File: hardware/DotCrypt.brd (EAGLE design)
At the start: 12 x 33.1 mm, 15 parts, among them CN1 1X4-BIG, U1 ATMEGA328P-MU-QFN32, U3 ATSHA204-TSU

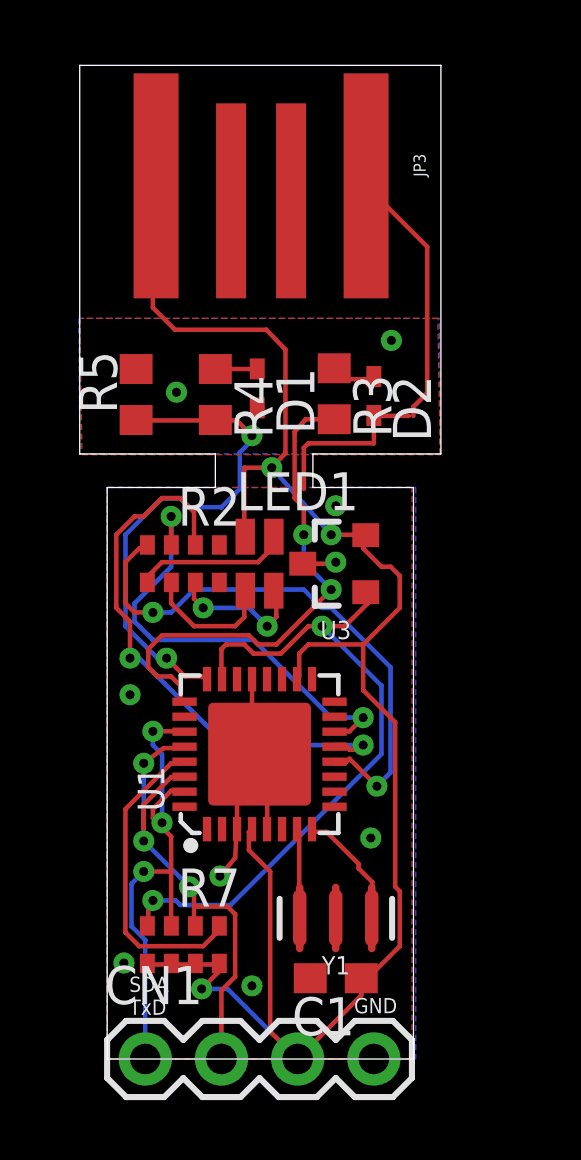
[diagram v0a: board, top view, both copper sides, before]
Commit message: Rearrange logos and pin connections
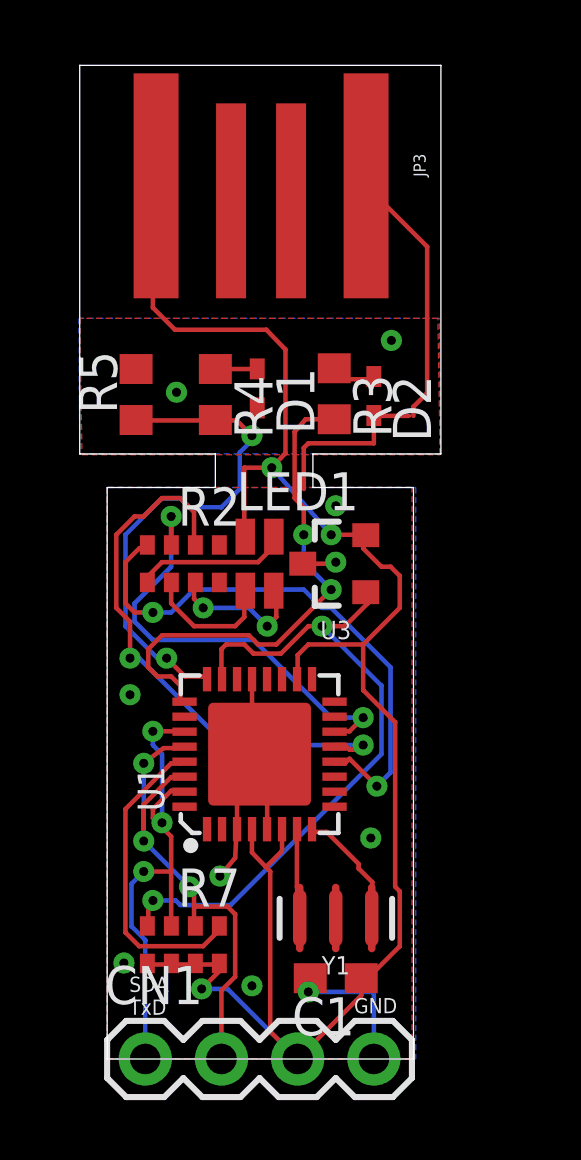
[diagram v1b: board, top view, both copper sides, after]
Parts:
- moved LOGO1 2.52 mm to (5.08, 5.77)
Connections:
- net +3V3: now also U1.6
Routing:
- net GND: track 26.4 -> 31.3 mm, vias 9 -> 10
- net +3V3: track 61.9 -> 63.3 mm
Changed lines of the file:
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@@
 <layer number="155" name="FabDoc3" color="7" fill="15" visible="no" active="no"/>
 <layer number="199" name="Contour" color="7" fill="1" visible="no" active="yes"/>
-<layer number="200" name="200bmp" color="1" fill="10" visible="yes" active="yes"/>
+<layer number="200" name="200bmp" color="1" fill="10" visible="no" active="yes"/>
 <layer number="201" name="201bmp" color="2" fill="1" visible="no" active="no"/>
 <layer number="202" name="202bmp" color="3" fill="1" visible="no" active="no"/>
@@
 TxD</text>
 <text x="8.2296" y="2.794" size="0.508" layer="21">GND</text>
-<text x="0" y="18.8722" size="0.508" layer="22" rot="MR180">DotCrypt v0.1.1</text>
-<text x="1.27" y="17.907" size="0.508" layer="22" rot="MR180">01/2018</text>
+<text x="9.4996" y="7.4168" size="0.508" layer="22" rot="SMR270">01/2018</text>
+<text x="7.4676" y="5.7658" size="0.508" layer="22" rot="SMR270" align="center">DotCrypt
+v0.1.1</text>
 </plain>
 <attributes>
@@
 <element name="R5" library="rcl" package="R0603" value="1.5kΩ" x="0.9652" y="23.4188" rot="R90"/>
 <element name="JP3" library="Spark" package="USB-A-PCB" value="USBPCB" x="5.1308" y="30.1752" rot="R270"/>
-<element name="LOGO1" library="SparkFun-Aesthetics" package="OSHW-LOGO-S" value="OSHW-LOGOS" x="7.5946" y="5.9436" rot="MR270"/>
+<element name="LOGO1" library="SparkFun-Aesthetics" package="OSHW-LOGO-S" value="OSHW-LOGOS" x="5.08" y="5.7658" rot="MR270"/>
 </elements>
 <signals>
@@
 <wire x1="8.89" y1="21.7932" x2="8.89" y2="22.7188" width="0.1524" layer="1"/>
 <wire x1="10.2108" y1="22.7076" x2="10.2108" y2="23.0124" width="0.1524" layer="1"/>
+<wire x1="6.77" y1="3.9624" x2="6.7056" y2="3.9624" width="0.1524" layer="1"/>
+<wire x1="6.7056" y1="3.9624" x2="6.7056" y2="3.5052" width="0.1524" layer="1"/>
+<via x="6.7056" y="3.5052" extent="1-16" drill="0.3"/>
+<wire x1="6.7056" y1="3.5052" x2="8.89" y2="3.5052" width="0.1524" layer="16"/>
+<wire x1="8.89" y1="3.5052" x2="8.89" y2="1.27" width="0.1524" layer="16"/>
 </signal>
 <signal name="SCK">
@@
 <contactref element="C1" pad="1"/>
 <contactref element="JP3" pad="5V"/>
-<wire x1="6.4008" y1="14.7828" x2="6.4008" y2="14.0208" width="0.1524" layer="1"/>
-<wire x1="6.7056" y1="15.0876" x2="6.4008" y2="14.7828" width="0.1524" layer="1"/>
+<wire x1="6.35" y1="14.732" x2="6.35" y2="14.0208" width="0.1524" layer="1"/>
+<wire x1="6.7056" y1="15.0876" x2="6.35" y2="14.732" width="0.1524" layer="1"/>
 <wire x1="8.5344" y1="15.0876" x2="6.7056" y2="15.0876" width="0.1524" layer="1"/>
 <wire x1="9.7536" y1="16.3068" x2="8.5344" y2="15.0876" width="0.1524" layer="1"/>
@@
 <wire x1="8.5344" y1="18.288" x2="9.144" y2="17.6784" width="0.1524" layer="1"/>
 <wire x1="8.5344" y1="18.5928" x2="8.5344" y2="18.288" width="0.1524" layer="1"/>
-<wire x1="6.4008" y1="14.0208" x2="6.33" y2="13.93" width="0.1524" layer="1"/>
+<wire x1="6.35" y1="14.0208" x2="6.33" y2="13.93" width="0.1524" layer="1"/>
 <wire x1="8.5344" y1="18.5928" x2="8.62" y2="18.73" width="0.1524" layer="1"/>
 <wire x1="2.1336" y1="4.4196" x2="1.3716" y2="4.4196" width="0.1524" layer="1"/>
@@
 <wire x1="3.6576" y1="4.4196" x2="3.74" y2="4.455" width="0.1524" layer="1"/>
 <wire x1="3.048" y1="4.4196" x2="2.94" y2="4.455" width="0.1524" layer="1"/>
-<wire x1="4.7244" y1="8.8392" x2="4.83" y2="8.93" width="0.1524" layer="1"/>
+<wire x1="4.826" y1="8.763" x2="4.83" y2="8.93" width="0.1524" layer="1"/>
 <wire x1="3.81" y1="4.4196" x2="3.74" y2="4.455" width="0.1524" layer="1"/>
 <wire x1="6.2484" y1="1.6764" x2="7.0104" y2="1.6764" width="0.1524" layer="1"/>
@@
 <wire x1="6.2484" y1="1.6764" x2="6.2484" y2="1.3716" width="0.1524" layer="1"/>
 <wire x1="6.2484" y1="1.3716" x2="6.35" y2="1.27" width="0.1524" layer="1"/>
-<wire x1="4.7244" y1="8.8392" x2="4.7244" y2="8.2296" width="0.1524" layer="1"/>
-<wire x1="4.7244" y1="8.2296" x2="5.4356" y2="7.5184" width="0.1524" layer="1"/>
+<wire x1="4.826" y1="8.763" x2="4.826" y2="8.1534" width="0.1524" layer="1"/>
+<wire x1="4.826" y1="8.1534" x2="5.291446875" y2="7.668559375" width="0.1524" layer="1"/>
+<wire x1="5.291446875" y1="7.668559375" x2="5.4356" y2="7.5184" width="0.1524" layer="1"/>
 <wire x1="5.4356" y1="7.5184" x2="5.4356" y2="2.1844" width="0.1524" layer="1"/>
 <wire x1="5.4356" y1="2.1844" x2="6.35" y2="1.27" width="0.1524" layer="1"/>
@@
 <wire x1="5.9436" y1="21.463" x2="5.4864" y2="20.9804" width="0.1524" layer="1"/>
 <wire x1="5.9436" y1="24.9174" x2="5.9436" y2="21.463" width="0.1524" layer="1"/>
+<contactref element="U1" pad="6"/>
+<wire x1="5.83" y1="8.93" x2="5.83" y2="8.2071125" width="0.1524" layer="1"/>
+<wire x1="5.83" y1="8.2071125" x2="5.291446875" y2="7.668559375" width="0.1524" layer="1"/>
 </signal>
 <signal name="PUSH">
@@
 <contactref element="U1" pad="7"/>
 <contactref element="Y1" pad="3"/>
-<wire x1="6.4008" y1="7.0104" x2="6.4008" y2="8.8392" width="0.1524" layer="1"/>
-<wire x1="6.4008" y1="8.8392" x2="6.33" y2="8.93" width="0.1524" layer="1"/>
-<wire x1="6.4008" y1="7.0104" x2="6.42" y2="5.969" width="0.1524" layer="1"/>
+<wire x1="6.3246" y1="7.0104" x2="6.3246" y2="8.8392" width="0.1524" layer="1"/>
+<wire x1="6.3246" y1="8.8392" x2="6.33" y2="8.93" width="0.1524" layer="1"/>
+<wire x1="6.3246" y1="7.0104" x2="6.42" y2="5.969" width="0.1524" layer="1"/>
 </signal>
 <signal name="XTAL2">

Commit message: Add USB D+ D- connections
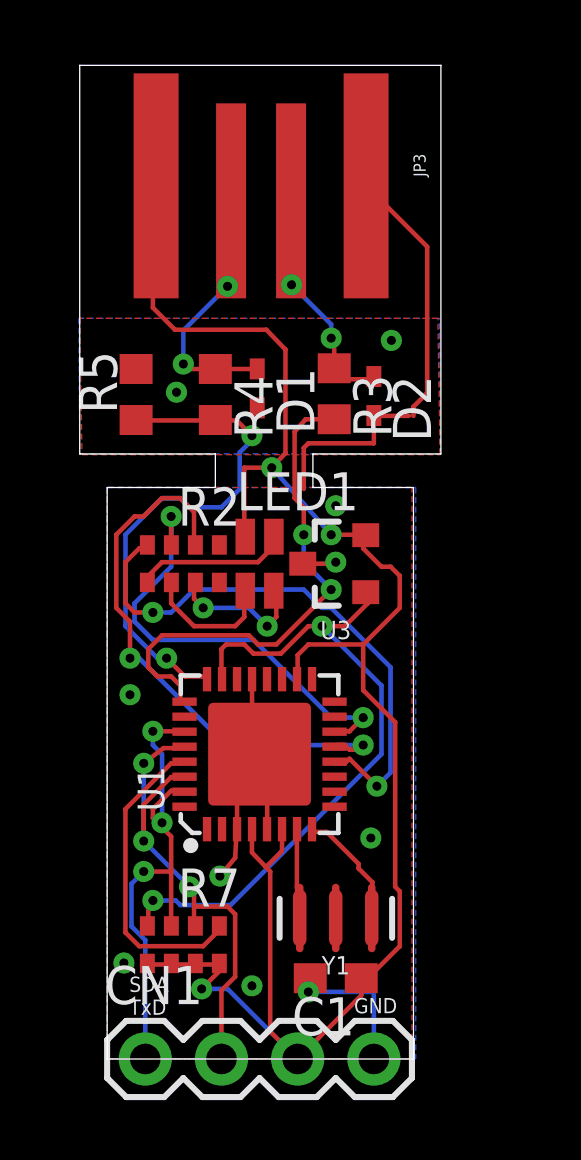
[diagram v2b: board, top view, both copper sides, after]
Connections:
- net USB_D+: now also JP3.USB_P
- net USB_D-: now also JP3.USB_M
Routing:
- net USB_D-: track 1.40 -> 8.63 mm, vias 0 -> 2
- net USB_D+: track 1.54 -> 7.72 mm, vias 0 -> 2
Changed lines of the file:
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@@
 <wire x1="3.6068" y1="24.2688" x2="4.9998" y2="24.2688" width="0.1524" layer="1"/>
 <wire x1="4.9998" y1="24.2688" x2="5.0038" y2="24.2728" width="0.1524" layer="1"/>
+<contactref element="JP3" pad="USB_M"/>
+<wire x1="3.6068" y1="24.2688" x2="2.706" y2="24.2688" width="0.1524" layer="1"/>
+<wire x1="2.706" y1="24.2688" x2="2.54" y2="24.4348" width="0.1524" layer="1"/>
+<via x="2.54" y="24.4348" extent="1-16" drill="0.3"/>
+<wire x1="2.54" y1="24.4348" x2="2.54" y2="25.5524" width="0.1524" layer="16"/>
+<wire x1="2.54" y1="25.5524" x2="4.0132" y2="27.0256" width="0.1524" layer="16"/>
+<via x="4.0132" y="27.0256" extent="1-16" drill="0.3"/>
+<wire x1="4.0132" y1="27.0256" x2="4.0132" y2="29.7576" width="0.1524" layer="1"/>
+<wire x1="4.0132" y1="29.7576" x2="4.1308" y2="29.8752" width="0.1524" layer="1"/>
 </signal>
 <signal name="USB_D+">
@@
 <wire x1="8.8392" y1="23.9268" x2="7.8858" y2="23.9268" width="0.1524" layer="1"/>
 <wire x1="7.8858" y1="23.9268" x2="7.5692" y2="24.2942" width="0.1524" layer="1"/>
+<contactref element="JP3" pad="USB_P"/>
+<wire x1="7.5692" y1="24.2942" x2="7.5692" y2="25.1968" width="0.1524" layer="1"/>
+<wire x1="7.5692" y1="25.1968" x2="7.4676" y2="25.2984" width="0.1524" layer="1"/>
+<via x="7.4676" y="25.2984" extent="1-16" drill="0.3"/>
+<wire x1="7.4676" y1="25.2984" x2="7.4676" y2="25.7556" width="0.1524" layer="16"/>
+<wire x1="7.4676" y1="25.7556" x2="6.1468" y2="27.0764" width="0.1524" layer="16"/>
+<via x="6.1468" y="27.0764" extent="1-16" drill="0.3"/>
+<wire x1="6.1468" y1="27.0764" x2="6.1468" y2="29.8592" width="0.1524" layer="1"/>
+<wire x1="6.1468" y1="29.8592" x2="6.1308" y2="29.8752" width="0.1524" layer="1"/>
 </signal>
 </signals>

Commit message: Add 3V3 regulator
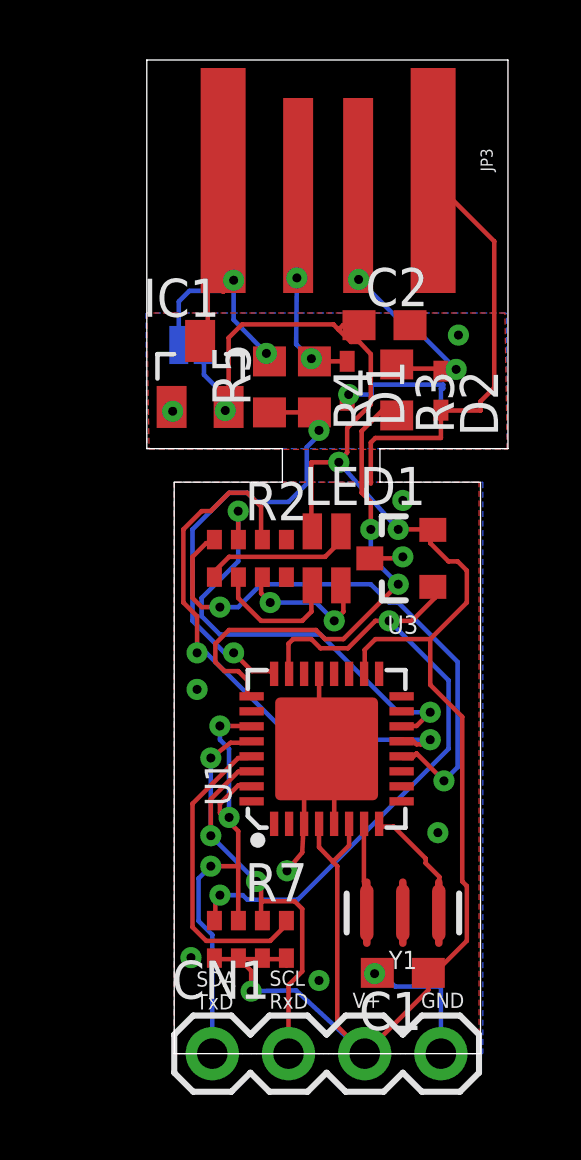
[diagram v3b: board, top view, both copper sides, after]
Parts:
- added C2: 1uF, rcl:C0603
- added IC1: MCP1703CB, linear:SOT23
- added JP1: JUMPER-SMT_2_NO_SILK, SparkFun-Jumpers:SMT-JUMPER_2_NO_SILK
- moved R5 4.45 mm to (5.41, 23.7)
- moved R4 3.31 mm to (6.91, 23.7)
- moved D1 3.01 mm to (8.00, 23.9)
- moved C1 2.24 mm to (9.86, 4.14)
- moved CN1 2.24 mm to (3.51, 1.45)
- moved JP3 2.24 mm to (7.37, 30.4)
- moved LED1 2.24 mm to (7.32, 18.0)
- moved LOGO1 2.24 mm to (7.32, 5.94)
- moved R2 2.24 mm to (4.78, 18.0)
- moved R7 2.24 mm to (4.78, 5.26)
- moved U1 2.24 mm to (7.32, 11.6)
- moved U3 2.24 mm to (9.86, 18.0)
- moved Y1 2.24 mm to (9.86, 6.15)
- moved D2 2.24 mm to (11.1, 23.6)
- moved R3 2.09 mm to (9.65, 23.6)
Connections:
- net +3V3: now also C2.1, IC1.2, JP1.1; no longer JP3.5V
- net +5V: now also IC1.3, JP1.2, JP3.5V
- net GND: now also C2.2, IC1.1
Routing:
- net +5V: track 0.00 -> 15.6 mm, vias 0 -> 2
- net GND: track 31.3 -> 36.0 mm, vias 10 -> 11
- net +3V3: track 63.3 -> 66.1 mm, vias 3 -> 4
- net USB_D+: track 7.72 -> 9.45 mm
- net USB_D-: track 8.63 -> 7.10 mm
- net D-: track 17.2 -> 16.0 mm
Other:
- board text added: "5V Logic"
- board text added: "SCL RxD"
- board text added: "V+"

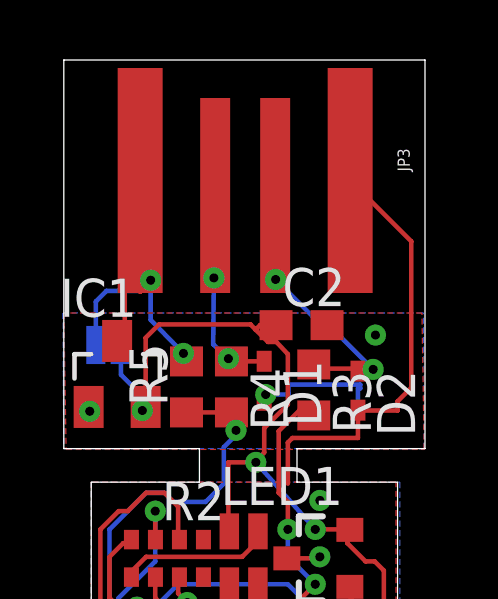
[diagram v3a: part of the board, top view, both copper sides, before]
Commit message: Reorder traces
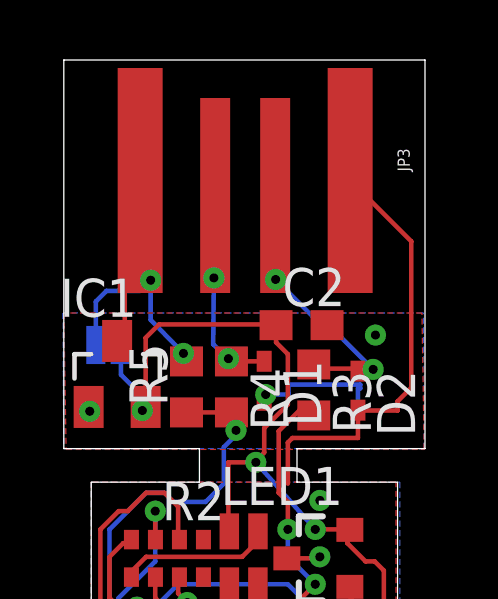
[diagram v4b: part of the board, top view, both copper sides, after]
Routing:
- net +5V: track 15.6 -> 12.5 mm
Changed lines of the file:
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@@
 <wire x1="10.7052" y1="4.1402" x2="10.7052" y2="3.5678" width="0.1524" layer="1"/>
 <wire x1="10.7052" y1="3.5678" x2="8.5852" y2="1.4478" width="0.1524" layer="1"/>
-<wire x1="4.4958" y1="25.7556" x2="7.5438" y2="25.7556" width="0.1524" layer="1"/>
-<wire x1="7.5438" y1="25.7556" x2="7.712678125" y2="25.579965625" width="0.1524" layer="1"/>
-<wire x1="7.712678125" y1="25.579965625" x2="8.128" y2="25.1714" width="0.1524" layer="1"/>
+<wire x1="4.4958" y1="25.7556" x2="8.3956" y2="25.7556" width="0.1524" layer="1"/>
 <wire x1="8.001" y1="21.4884" x2="7.7216" y2="21.1582" width="0.1524" layer="1"/>
 <contactref element="U1" pad="6"/>
@@
 <contactref element="C2" pad="1"/>
 <contactref element="IC1" pad="2"/>
-<wire x1="8.128" y1="25.1714" x2="8.4074" y2="25.1714" width="0.1524" layer="1"/>
-<wire x1="8.4074" y1="25.1714" x2="8.7884" y2="24.765" width="0.1524" layer="1"/>
 <wire x1="8.7884" y1="24.765" x2="8.7884" y2="23.0886" width="0.1524" layer="1"/>
 <wire x1="8.7884" y1="23.0886" x2="8.001" y2="22.3012" width="0.1524" layer="1"/>
@@
 <wire x1="4.4958" y1="25.7556" x2="4.0488" y2="25.3086" width="0.1524" layer="1"/>
 <wire x1="4.0488" y1="25.3086" x2="4.0488" y2="23.0046" width="0.1524" layer="1"/>
-<wire x1="8.3956" y1="25.7302" x2="7.865078125" y2="25.733078125" width="0.1524" layer="1"/>
-<wire x1="7.865078125" y1="25.733078125" x2="7.712678125" y2="25.579965625" width="0.1524" layer="1"/>
 <contactref element="JP1" pad="1"/>
 <wire x1="3.2004" y1="25.0698" x2="3.2258" y2="25.0698" width="0.1524" layer="16"/>
@@
 <wire x1="4.8006" y1="3.5306" x2="4.8006" y2="4.2074" width="0.1524" layer="1"/>
 <wire x1="4.8006" y1="4.2074" x2="4.3752" y2="4.6328" width="0.1524" layer="1"/>
+<wire x1="8.3956" y1="25.7556" x2="8.3956" y2="25.7302" width="0.1524" layer="1"/>
+<wire x1="8.7884" y1="24.765" x2="8.3956" y2="25.1578" width="0.1524" layer="1"/>
+<wire x1="8.3956" y1="25.1578" x2="8.3956" y2="25.7302" width="0.1524" layer="1"/>
 </signal>
 <signal name="PUSH">
@@
 <wire x1="4.2164" y1="25.908" x2="4.2164" y2="27.2288" width="0.1524" layer="16"/>
 <via x="4.2164" y="27.2288" extent="1-16" drill="0.3"/>
-<wire x1="4.2164" y1="27.2288" x2="3.866" y2="26.8426" width="0.1524" layer="1"/>
-<wire x1="3.866" y1="26.8426" x2="3.866" y2="29.4184" width="0.1524" layer="1"/>
 <contactref element="JP1" pad="2"/>
 <wire x1="2.3876" y1="25.0698" x2="2.3876" y2="26.5176" width="0.1524" layer="16"/>
@@
 <wire x1="2.7432" y1="26.8732" x2="3.8608" y2="26.8732" width="0.1524" layer="16"/>
 <wire x1="3.8608" y1="26.8732" x2="4.2164" y2="27.2288" width="0.1524" layer="16"/>
+<wire x1="2.3876" y1="25.0698" x2="3.0988" y2="25.2046" width="0" layer="19" extent="1-16"/>
 </signal>
 <signal name="USB_D-">
